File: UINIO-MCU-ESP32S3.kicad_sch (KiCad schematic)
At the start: 0 parts

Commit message: Start schematic drawing.
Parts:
- added AE?: Antenna_Chip, RF_Antenna:Texas_SWRA117D_2.4GHz_Right, symbol Device:Antenna_Chip
- added C? (x7): 1uF, Capacitor_SMD:C_0402_1005Metric, symbol Device:C
- added C? (x2): 15pF, Capacitor_SMD:C_0402_1005Metric, symbol Device:C
- added C?: 10uF, Capacitor_SMD:C_0402_1005Metric, symbol Device:C
- added C?: 10nF, Capacitor_SMD:C_0402_1005Metric, symbol Device:C
- added C? (x7): 0.1uF, Capacitor_SMD:C_0402_1005Metric, symbol Device:C
- added C? (x2): 0uF, Capacitor_SMD:C_0402_1005Metric, symbol Device:C
- added D?: LED_Red, LED_SMD:LED_0603_1608Metric, symbol Device:LED
- added J?: 外接串行下载接口, Connector_PinHeader_2.54mm:PinHeader_1x04_P2.54mm_Vertical, symbol Connector:Conn_01x04_Male
- added J? (x2): Conn_01x15_Male, Connector_PinHeader_2.54mm:PinHeader_1x15_P2.54mm_Vertical, symbol Connector:Conn_01x15_Male
- added L?: 0uH, Inductor_SMD:L_0402_1005Metric, symbol Device:L
- added R? (x4): 10K, Resistor_SMD:R_0402_1005Metric, symbol Device:R
- added R?: 2K, Resistor_SMD:R_0402_1005Metric, symbol Device:R
- added SW?: 下载按键, Uinio:KEY-SMD_4P-L4.2-W3.4-P2.15-LS4.7, symbol Uinio:Key_YTS_A016S_1
- added SW?: 复位按键, Uinio:KEY-SMD_4P-L4.2-W3.4-P2.15-LS4.7, symbol Uinio:Key_YTS_A016S_1
- added U?: W25Q128JVSSIQ, Uinio:SOIC-8_L5.3-W5.3-P1.27-LS8.0-BL, symbol Uinio:W25Q128JVSSIQ
- added U?: ME6211C33M5G-N, Uinio:SOT-23-5_L3.0-W1.7-P0.95-LS2.8-BR, symbol Uinio:ME6211
- added U?: ESP32-S3, Uinio:ESP32-S3, symbol Uinio:ESP32-S3
- added U?: CH343P, Uinio:TQFN-16_L3.0-W3.0-P0.50-BL-EP1.7, symbol Uinio:CH343P
- added USB?: USB_Type_C_16Pin, Uinio:USB-C-SMD_TYPEC-304J-BCP16, symbol Uinio:USB_Type_C_16Pin
- added VT? (x2): S8050, Uinio:SOT-23-3_L2.9-W1.6-P1.90-LS2.9-BL, symbol Uinio:S8050
- added Y?: 40MHz, Crystal:Crystal_SMD_3225-4Pin_3.2x2.5mm, symbol Device:Crystal_GND24
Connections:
- new net: C?.2, U?.53 (XTAL_N), Y?.3
- new net: AE?.1 (FEED), C?.1, L?.1
- new net: R?.2, VT?.1 (B) (x2)
- new net: C?.2, U?.54 (XTAL_P), Y?.1
- new net: D?.2 (A), R?.1
- new net: C?.1, L?.2, U?.1 (LNA_IN)
- new net CHIP_EN: J?.5 (Pin_5), SW?.3, SW?.4, VT?.3 (C)
- new net CHIP_PU: C?.1, R?.2, U?.4 (CHIP_PU)
- new net DTR: J?.1 (Pin_1), R?.1, U?.12 (DTRTNOW), VT?.2 (E)
- new net GND: AE?.2 (PCB_Trace), C?.1, C?.1, C?.1, C?.1, C?.1, C?.1, C?.2, C?.2, C?.2, C?.2, C?.2, C?.2, C?.2, C?.2, C?.2, C?.2, C?.2, C?.2, C?.2, C?.2, D?.1 (K), J?.1 (Pin_1), J?.1 (Pin_1), J?.14 (Pin_14), J?.14 (Pin_14), SW?.1, SW?.1, SW?.2, SW?.2, U?.17 (EP), U?.2 (GND), U?.2 (Vss), U?.4 (GND), U?.57 (GND), USB?.13 (GND), USB?.14 (GND), USB?.15 (GND), USB?.16 (GND), USB?.A1B12 (GND), USB?.B1A12 (GND), Y?.2, Y?.4
- new net GPIO0: U?.5 (GPIO0)
- new net GPIO0/U1TXD: J?.2 (Pin_2)
- new net GPIO1: U?.6 (GPIO1)
- new net GPIO10: J?.13 (Pin_13), U?.15 (GPIO10)
- new net GPIO11: U?.16 (GPIO11)
- new net GPIO12: U?.17 (GPIO12)
- new net GPIO13: U?.18 (GPIO13)
- new net GPIO14: U?.19 (GPIO14)
- new net GPIO15: U?.21 (XTAL_32K_P)
- new net GPIO16: U?.22 (XTAL_32K_N)
- new net GPIO17: U?.23 (GPIO17)
- new net GPIO18: U?.24 (GPIO18)
- new net GPIO18/USB_D-: J?.6 (Pin_6)
- new net GPIO19/USB_D+: J?.5 (Pin_5)
- new net GPIO19/USB_D-: U?.25 (GPIO19)
- new net GPIO1/U1RXD: J?.3 (Pin_3)
- new net GPIO2: J?.4 (Pin_4), U?.7 (GPIO2)
- new net GPIO20/USB_D+: U?.26 (GPIO20)
- new net GPIO21: U?.27 (GPIO21)
- new net GPIO3: J?.6 (Pin_6), U?.8 (GPIO3)
- new net GPIO33: U?.38 (GPIO33)
- new net GPIO34: U?.39 (GPIO34)
- new net GPIO35: U?.40 (GPIO35)
- new net GPIO36: U?.41 (GPIO36)
- new net GPIO37: U?.42 (GPIO37)
- new net GPIO38: U?.43 (GPIO38)
- new net GPIO39: U?.44 (MTCK)
- new net GPIO4: U?.9 (GPIO4)
- new net GPIO40: U?.45 (MTD0)
- new net GPIO41: U?.47 (MTDI)
- new net GPIO42: U?.48 (MTMS)
- new net GPIO45: U?.51 (GPIO45)
- new net GPIO46: U?.52 (GPIO46)
- new net GPIO4/ADC1/SDA: J?.8 (Pin_8)
- new net GPIO5: U?.10 (GPIO5)
- new net GPIO5/ADC2/SCL: J?.7 (Pin_7)
- new net GPIO6: J?.9 (Pin_9), U?.11 (GPIO6)
- new net GPIO7: J?.10 (Pin_10), U?.12 (GPIO7)
- new net GPIO8: U?.13 (GPIO8)
- new net GPIO8/PWM: J?.11 (Pin_11)
- new net GPIO9: U?.14 (GPIO9)
- new net GPIO9/BOOT: J?.12 (Pin_12), R?.1, SW?.3, SW?.4, VT?.3 (C)
- new net RTS: J?.4 (Pin_4), R?.1, U?.13 (RTS), VT?.2 (E)
- new net SPICLK: J?.9 (Pin_9)
- new net SPICLK_N/GPIO48: U?.36 (SPICLK_N)
- new net SPICLK_P/GPIO47: U?.37 (SPICLK_P)
- new net SPICLK/GPIO30: U?.33 (SPICLK), U?.6 (CLK)
- new net SPICS0: J?.10 (Pin_10)
- new net SPICS0/GPIO29: U?.1 (CS#), U?.32 (SPICS0)
- new net SPICS1/GPIO26: U?.28 (SPICS1)
- new net SPID: J?.8 (Pin_8)
- new net SPID/GPIO32: U?.35 (SPID), U?.5 (DI(IO0))
- new net SPIHD/GPIO12: J?.12 (Pin_12)
- new net SPIHD/GPIO27: U?.30 (SPIHD)
- new net SPIQ: J?.7 (Pin_7)
- new net SPIQ/GPIO31: U?.2 (DO(IO1)), U?.34 (SPIQ)
- new net SPIWP/GPIO13: J?.11 (Pin_11)
- new net SPIWP/GPIO28: U?.31 (SPIWP)
- new net U0RXD: J?.2 (Pin_2), J?.4 (Pin_4), U?.4 (TXD), U?.50 (U0RXD)
- new net U0TXD: J?.3 (Pin_3), J?.3 (Pin_3), U?.49 (U0TXD), U?.5 (RXD)
- new net USB_Data+: U?.7 (UD+), USB?.A6 (DP1), USB?.B6 (DP2)
- new net USB_Data-: U?.8 (UD-), USB?.A7 (DN1), USB?.B7 (DN2)
- new net VDD_3.3V: C?.1, C?.1, C?.1, C?.1, C?.1, C?.1, C?.1, C?.1, C?.1, C?.2, C?.2, J?.15 (Pin_15), J?.2 (Pin_2), R?.1, R?.2, R?.2, U?.1 (VIO), U?.2 (VDD3P3), U?.20 (VDD3P3_RTC), U?.3 (VDD3P3), U?.3 (WP#(IO2)), U?.46 (VDD3P3_CPU), U?.5 (Vout), U?.55 (VDDA), U?.56 (VDDA), U?.6 (V3), U?.7 (HOLD#/RESET#/(IO3)), U?.8 (VCC)
- new net VDD_5V: C?.2, C?.2, J?.15 (Pin_15), U?.1 (Vin), U?.3 (CE), U?.3 (VDD5), U?.9 (VBUS), USB?.A4B9 (VBUS), USB?.B4A9 (VBUS)
- new net VDD_SPI/GPIO11: C?.1, C?.1, J?.13 (Pin_13), U?.29 (VDD_SPI)
- no-connect marks 0 -> 10
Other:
- note added: "2.54mm 排针"
- note added: "3.3V 线性稳压电路"
- note added: "CH343 USB 转 UART 电路"
- note added: "ESP32-C3 最小系统"
- note added: "Flash 存储器电路"
- note added: "USB Type-C 接口电路"
- note added: "下载控制电路"

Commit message: Start schematic drawing.
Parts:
- removed J? (x2): Conn_01x15_Male, Connector_PinHeader_2.54mm:PinHeader_1x15_P2.54mm_Vertical, symbol Connector:Conn_01x15_Male
- removed R? (x3): 10K, Resistor_SMD:R_0402_1005Metric, symbol Device:R
- removed SW?: 下载按键, Uinio:KEY-SMD_4P-L4.2-W3.4-P2.15-LS4.7, symbol Uinio:Key_YTS_A016S_1
- removed SW?: 复位按键, Uinio:KEY-SMD_4P-L4.2-W3.4-P2.15-LS4.7, symbol Uinio:Key_YTS_A016S_1
- removed VT? (x2): S8050, Uinio:SOT-23-3_L2.9-W1.6-P1.90-LS2.9-BL, symbol Uinio:S8050
- added C? (x2): 0.1uF, Capacitor_SMD:C_0402_1005Metric, symbol Device:C
- added Card?: TF_Card_02A, Uinio:TF-SMD_TF-02, symbol Uinio:TF_Card_02A
- added J? (x2): Conn_01x28_Male, symbol Connector:Conn_01x28_Male
- added R? (x2): 5.1K, Resistor_SMD:R_0402_1005Metric, symbol Device:R
- added R? (x3): 10K, Resistor_SMD:R_0402_1005Metric, symbol Device:R
- added SW?: SWITCH_SS12D00G3, Uinio:SW-TH_SS-12D01-GX, symbol Uinio:SWITCH_SS12D00G3
- added U?: ESP-PSRAM64H, Uinio:SOP-8_L4.9-W3.9-P1.27-LS6.0-BL, symbol Uinio:ESP-PSRAM64H
- added U?: RS2227XUTQK10, Uinio:WQFN-10_L1.8-W1.4-P0.40-BL, symbol Uinio:RS2227XUTQK10
- added U?: LMBT3904DW1T1G, Uinio:SOT-363_L2.0-W1.3-P0.65-LS2.1-TL, symbol Uinio:LMBT3904DW1T1G
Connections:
- net CHIP_PU: now also U?.6 (C)
- net DTR: now also R?.1, U?.4 (E)
- net GND: now also C?.1, C?.2, Card?.10 (GND), Card?.11 (GND), Card?.12 (GND), Card?.13 (GND), Card?.6 (VSS), R?.2, R?.2, SW?.1, U?.3 (GND), U?.8 (OE#)
- net GPIO0: now also U?.3 (C)
- net RTS: now also R?.2, U?.1 (E)
- net SPICLK/GPIO30: now also U?.6 (SCLK)
- net SPICS1/GPIO26: now also U?.1 (CE#)
- net SPID/GPIO32: now also U?.5 (SI/SIO0)
- net SPIHD/GPIO27: now also U?.7 (SIO3)
- net SPIQ/GPIO31: now also U?.2 (SO/SIO1)
- net SPIWP/GPIO28: now also U?.3 (SIO2)
- net USB_Data+: now also U?.1 (D+); no longer U?.7 (UD+)
- net USB_Data-: now also U?.2 (D-); no longer U?.8 (UD-)
- net VDD_5V: now also R?.2
- net at USB?.A5 (CC1): now also R?.1
- net at USB?.B5 (CC2): now also R?.1
- net GPIO19/USB_D- renamed ESP_USB_D+
- net ESP_USB_D+: now also U?.4 (HSD1-)
- net GPIO20/USB_D+ renamed ESP_USB_D-
- net ESP_USB_D-: now also U?.5 (HSD1+)
- new net: SW?.2, U?.10 (S)
- new net: R?.1, SW?.3
- new net: C?.1, U?.4 (VSS), U?.8 (VCC)
- new net: R?.1, U?.5 (B)
- new net: R?.2, U?.2 (B)
- new net CH_USB_Data+: U?.7 (HSD2+), U?.7 (UD+)
- new net CH_USB_Data-: U?.6 (HSD2-), U?.8 (UD-)
- new net VBUS: C?.2, U?.9 (V+)
- no-connect marks 10 -> 11
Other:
- note added: "PSRAM 存储器电路"
- note added: "UART0 下载控制电路"
- note added: "引脚排针"
- note removed: "2.54mm 排针"
- note removed: "下载控制电路"
- moved on the sheet: AE?, C?, D?, J?, L?, R?, U?, USB?, Y?

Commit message: Update PCB.
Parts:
- added R?: 10K, Resistor_SMD:R_0402_1005Metric, symbol Device:R
- C? (x2): value 0uF -> TBD
- L?: value 0uH -> TBD
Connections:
- net GPIO45: now also R?.2
- net VDD_3.3V: now also R?.1
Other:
- moved on the sheet: C?, Y?

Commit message: Complete schematic drawing.
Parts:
- removed C?: 1uF, Capacitor_SMD:C_0402_1005Metric, symbol Device:C
- removed C?: 0.1uF, Capacitor_SMD:C_0402_1005Metric, symbol Device:C
- removed Card?: TF_Card_02A, Uinio:TF-SMD_TF-02, symbol Uinio:TF_Card_02A
- removed J? (x2): Conn_01x28_Male, symbol Connector:Conn_01x28_Male
- removed J?: 外接串行下载接口, Connector_PinHeader_2.54mm:PinHeader_1x04_P2.54mm_Vertical, symbol Connector:Conn_01x04_Male
- removed SW?: SWITCH_SS12D00G3, Uinio:SW-TH_SS-12D01-GX, symbol Uinio:SWITCH_SS12D00G3
- removed U?: ESP-PSRAM64H, Uinio:SOP-8_L4.9-W3.9-P1.27-LS6.0-BL, symbol Uinio:ESP-PSRAM64H
- added J1: Conn_01x03_Pin, Connector_PinHeader_2.54mm:PinHeader_1x03_P2.54mm_Vertical, symbol Connector:Conn_01x03_Pin
- added J2, J4: Conn_01x27_Pin, Connector_PinHeader_2.54mm:PinHeader_1x27_P2.54mm_Vertical, symbol Connector:Conn_01x27_Pin
- added J3: Conn_01x04_Pin, Connector_PinHeader_2.54mm:PinHeader_1x04_P2.54mm_Vertical, symbol Connector:Conn_01x04_Pin
- added R9: 10K, Resistor_SMD:R_0402_1005Metric, symbol Device:R
- added SW1: 复位, Uinio:KEY-SMD_4P-L4.2-W3.4-P2.15-LS4.7, symbol Uinio:Key_YTS_A016S_1
- added SW2: 启动选择, Uinio:KEY-SMD_4P-L4.2-W3.4-P2.15-LS4.7, symbol Uinio:Key_YTS_A016S_1
- added U3: ESP-PSRAM64H, Uinio:SOP-8_L4.9-W3.9-P1.27-LS6.0-BL, symbol Uinio:ESP-PSRAM64H
- gave numbers to parts that had none: 39
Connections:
- net VBUS is gone; now on net VDD_3.3V: C11.2, U4.9 (V+)
- net CHIP_PU: now also SW1.3, SW1.4
- net DTR: now also J3.1 (Pin_1)
- net GND: now also J1.1 (Pin_1), J2.1 (Pin_1), J2.27 (Pin_27), J4.1 (Pin_1), J4.27 (Pin_27), J4.3 (Pin_3), SW1.1, SW1.2, SW2.1, SW2.2, U3.4 (VSS)
- net GPIO0: now also J2.3 (Pin_3), R9.1, SW2.3, SW2.4
- net GPIO1: now also J2.4 (Pin_4)
- net GPIO10: now also J2.13 (Pin_13)
- net GPIO11: now also J2.14 (Pin_14)
- net GPIO12: now also J2.15 (Pin_15)
- net GPIO13: now also J2.16 (Pin_16)
- net GPIO14: now also J2.17 (Pin_17)
- net GPIO15: now also J2.18 (Pin_18)
- net GPIO16: now also J2.19 (Pin_19)
- net GPIO17: now also J2.20 (Pin_20)
- net GPIO18: now also J2.21 (Pin_21)
- net GPIO2: now also J2.5 (Pin_5)
- net GPIO21: now also J2.24 (Pin_24)
- net GPIO3: now also J2.6 (Pin_6)
- net GPIO33: now also J4.12 (Pin_12)
- net GPIO34: now also J4.13 (Pin_13)
- net GPIO35: now also J4.14 (Pin_14)
- net GPIO36: now also J4.15 (Pin_15)
- net GPIO37: now also J4.16 (Pin_16)
- net GPIO38: now also J4.11 (Pin_11)
- net GPIO39: now also J4.10 (Pin_10)
- net GPIO4: now also J2.7 (Pin_7)
- net GPIO40: now also J4.9 (Pin_9)
- net GPIO41: now also J4.8 (Pin_8)
- net GPIO42: now also J4.7 (Pin_7)
- net GPIO45: now also J4.6 (Pin_6)
- net GPIO46: now also J4.5 (Pin_5)
- net GPIO5: now also J2.8 (Pin_8)
- net GPIO6: now also J2.9 (Pin_9)
- net GPIO7: now also J2.10 (Pin_10)
- net GPIO8: now also J2.11 (Pin_11)
- net GPIO9: now also J2.12 (Pin_12)
- net RTS: now also J3.4 (Pin_4)
- net SPICLK_N/GPIO48: now also J4.18 (Pin_18)
- net SPICLK_P/GPIO47: now also J4.17 (Pin_17)
- net SPICLK/GPIO30: now also J4.21 (Pin_21), U3.6 (SCLK)
- net SPICS0/GPIO29: now also J4.22 (Pin_22)
- net SPICS1/GPIO26: now also J2.25 (Pin_25), U3.1 (CE#)
- net SPID/GPIO32: now also J4.19 (Pin_19), U3.5 (SI/SIO0)
- net SPIHD/GPIO27: now also U2.7 (HOLD#/RESET#/(IO3)), J4.24 (Pin_24), U3.7 (SIO3)
- net SPIQ/GPIO31: now also J4.20 (Pin_20), U3.2 (SO/SIO1)
- net SPIWP/GPIO28: now also U2.3 (WP#(IO2)), J4.23 (Pin_23), U3.3 (SIO2)
- net U0RXD: now also J3.2 (Pin_2)
- net U0TXD: now also J3.3 (Pin_3)
- net VDD_3.3V: now also R5.2, J2.2 (Pin_2), J2.26 (Pin_26), J4.26 (Pin_26), J4.4 (Pin_4), R9.2; no longer U2.3 (WP#(IO2)), U2.7 (HOLD#/RESET#/(IO3)), U2.8 (VCC)
- net VDD_5V: now also J4.2 (Pin_2); no longer R5.2
- net VDD_SPI/GPIO11: now also U2.8 (VCC), J4.25 (Pin_25), U3.8 (VCC)
- net at U4.10 (S): now also J1.2 (Pin_2)
- net at R5.1: now also J1.3 (Pin_3)
- net CH_USB_Data+ renamed CH343_USB_Data+
- net CH_USB_Data- renamed CH343_USB_Data-
- net ESP_USB_D+ renamed GPIO19/ESP32_USB_D-
- net GPIO19/ESP32_USB_D-: now also J2.22 (Pin_22)
- net ESP_USB_D- renamed GPIO20/ESP32_USB_D+
- net GPIO20/ESP32_USB_D+: now also J2.23 (Pin_23)
- no-connect marks 11 -> 8
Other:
- note added: "2.54mm 间距引脚排针"
- note added: "PSRAM 伪静态随机存储器"
- note added: "USB - UART0 下载控制电路"
- note added: "复位与启动选择按键"
- note removed: "CH343 USB 转 UART 电路"
- note removed: "PSRAM 存储器电路"
- note removed: "UART0 下载控制电路"
- note removed: "引脚排针"
- moved on the sheet: AE1, C1, C10, C11, C12, C13, C14, C15, C16, C17, C18, C19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

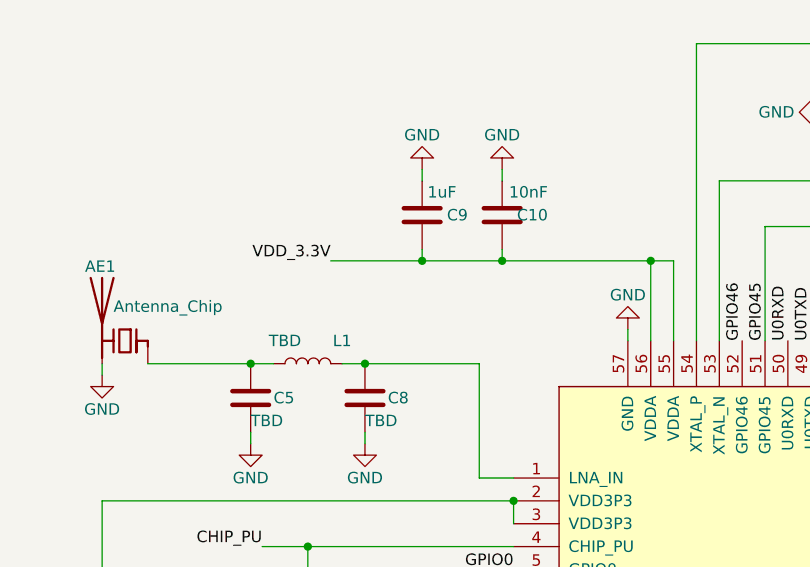
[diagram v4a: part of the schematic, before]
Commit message: PCB layout finish.
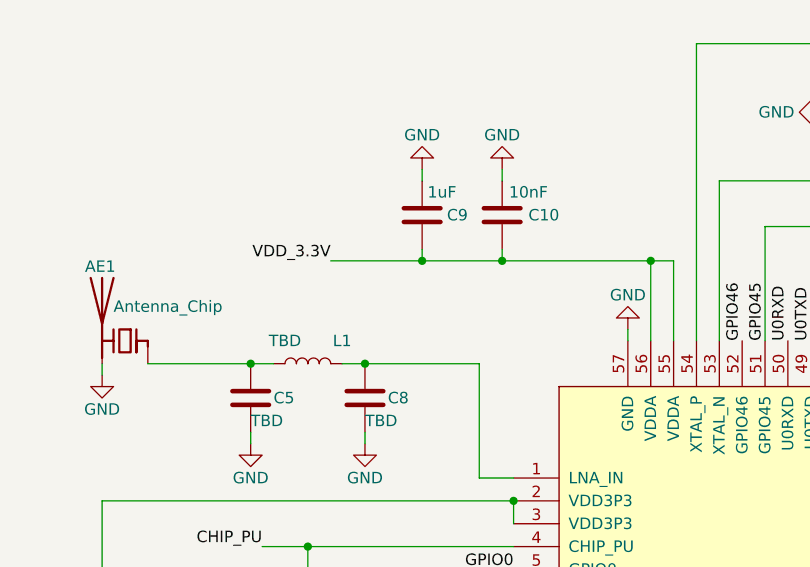
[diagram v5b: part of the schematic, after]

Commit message: Update PCB layout.
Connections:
- net GND: now also J4.25 (Pin_25); no longer J4.3 (Pin_3)
- net GPIO33: now also J4.14 (Pin_14); no longer J4.12 (Pin_12)
- net GPIO35: now also J4.12 (Pin_12); no longer J4.14 (Pin_14)
- net GPIO36: now also J4.10 (Pin_10); no longer J4.15 (Pin_15)
- net GPIO37: now also J4.11 (Pin_11); no longer J4.16 (Pin_16)
- net GPIO38: now also J4.9 (Pin_9); no longer J4.11 (Pin_11)
- net GPIO39: now also J4.8 (Pin_8); no longer J4.10 (Pin_10)
- net GPIO40: now also J4.7 (Pin_7); no longer J4.9 (Pin_9)
- net GPIO41: now also J4.6 (Pin_6); no longer J4.8 (Pin_8)
- net GPIO42: now also J4.5 (Pin_5); no longer J4.7 (Pin_7)
- net GPIO45: now also J4.4 (Pin_4); no longer J4.6 (Pin_6)
- net GPIO46: now also J4.3 (Pin_3); no longer J4.5 (Pin_5)
- net SPICLK_N/GPIO48: now also J4.16 (Pin_16); no longer J4.18 (Pin_18)
- net SPICLK_P/GPIO47: now also J4.15 (Pin_15); no longer J4.17 (Pin_17)
- net SPICLK/GPIO30: now also J4.19 (Pin_19); no longer J4.21 (Pin_21)
- net SPICS0/GPIO29: now also J4.20 (Pin_20); no longer J4.22 (Pin_22)
- net SPID/GPIO32: now also J4.17 (Pin_17); no longer J4.19 (Pin_19)
- net SPIHD/GPIO27: now also J4.22 (Pin_22); no longer J4.24 (Pin_24)
- net SPIQ/GPIO31: now also J4.18 (Pin_18); no longer J4.20 (Pin_20)
- net SPIWP/GPIO28: now also J4.21 (Pin_21); no longer J4.23 (Pin_23)
- net VDD_3.3V: now also J4.2 (Pin_2), J4.24 (Pin_24); no longer J4.26 (Pin_26), J4.4 (Pin_4)
- net VDD_5V: now also J4.26 (Pin_26); no longer J4.2 (Pin_2)
- net VDD_SPI/GPIO11: now also J4.23 (Pin_23); no longer J4.25 (Pin_25)

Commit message: Start wiring.
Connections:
- net GPIO36: now also J4.11 (Pin_11); no longer J4.10 (Pin_10)
- net GPIO37: now also J4.10 (Pin_10); no longer J4.11 (Pin_11)
- net U0RXD: now also J3.3 (Pin_3); no longer J3.2 (Pin_2)
- net U0TXD: now also J3.2 (Pin_2); no longer J3.3 (Pin_3)
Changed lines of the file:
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@@
     (effects (font (size 1.27 1.27)) (justify right bottom))
   )
-  (label "U0RXD" (at 384.81 222.25 0) (fields_autoplaced)
+  (label "U0RXD" (at 384.81 224.79 0) (fields_autoplaced)
     (effects (font (size 1.27 1.27)) (justify left bottom))
   )
@@
     (effects (font (size 1.27 1.27)) (justify right bottom))
   )
-  (label "U0TXD" (at 384.81 224.79 0) (fields_autoplaced)
+  (label "U0TXD" (at 384.81 222.25 0) (fields_autoplaced)
     (effects (font (size 1.27 1.27)) (justify left bottom))
   )
@@
     (effects (font (size 1.27 1.27)) (justify left bottom))
   )
-  (label "GPIO36" (at 379.73 53.34 180) (fields_autoplaced)
+  (label "GPIO36" (at 379.73 55.88 180) (fields_autoplaced)
     (effects (font (size 1.27 1.27)) (justify right bottom))
   )
@@
     (effects (font (size 1.27 1.27)) (justify right bottom))
   )
-  (label "GPIO37" (at 379.73 55.88 180) (fields_autoplaced)
-    (effects (font (size 1.27 1.27)) (justify right bottom))
-  )
+  (label "GPIO37" (at 379.73 53.34 180) (fields_autoplaced)
+    (effects (font (size 1.27 1.27)) (justify right bottom))
+  )
